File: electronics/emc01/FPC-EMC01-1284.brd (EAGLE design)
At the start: 160 x 100 mm, 87 parts, among them J10 CON-FFC-SFW15R, J4 PCIE, J9 CON-HDMI, Q4 16Mhz, SW1 SPST_TACT-EVQQ2, U1 LM2841, U10 MCP4728, U2 A4982, U3 A4982, U4 A4982, U5 ATMEGA1284P-AU, U7 AP7313

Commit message: Added pcb outline for FPC-EMC01-1284.brd, and placed connectors per AutoCAD DXF.  Added male 16-pin connector to firepick.lbr.
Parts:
- removed J3: (no value), pinhead-2:2X08SMD
- removed JP1: MOT-Y, SRG:JST_B4B-PH_HEADER
- removed JP10, JP11, JP8: (no value), pinhead-2:1X03SMD/90
- removed JP2: ICSP, pinhead-2:2X03SMD
- removed JP3: MOT-Z, SRG:JST_B4B-PH_HEADER
- removed JP4: (no value), pinhead-2:2X13SMD
- removed JP9: MOT-X, SRG:JST_B4B-PH_HEADER
- added J11, J12, J13, J14, J15: CONN-RECT-16PIN-2ROW, FirePick:CONN-RECT-2.54MM-16PIN-2ROW-SMTH
- added J2: PCIE, printrbot:5566-6
- added J8: CONN-RECT-3PINJST_PH_2MM, FirePick:CONN-JST_PH-2.0MM-3PIN-SMT-RA
- J1: value (none) -> CONN-RECT-26PIN-2ROWSHROUDED; device pinhead-2:2X08SMD -> FirePick:CONN-RECT-2.54MM-26-PIN-ROW-SHROUDED-SMTH
- J10: value CON-FFC-SFW15R -> ICSP; device !NJ SMT:CON-FFC-SFW15R -> FirePick:CONN-RECT-2.54MM-6-PIN-2ROW-SMTH
- J4: value PCIE -> MOT-X; device printrbot:5566-6 -> FirePick:CONN-JST-PH_2.0MM_4PIN-SMT-RA
- J5: value (none) -> MOT-Y; device pinhead-2:2X08SMD -> FirePick:CONN-JST-PH_2.0MM_4PIN-SMT-RA
- J6: value (none) -> MOT-Z; device pinhead-2:2X08SMD -> FirePick:CONN-JST-PH_2.0MM_4PIN-SMT-RA
- J7: value (none) -> CONN-RECT-3PINJST_PH_2MM; device pinhead-2:2X08SMD -> FirePick:CONN-JST_PH-2.0MM-3PIN-SMT-RA
- J9: value CON-HDMI -> CONN-RECT-3PINJST_PH_2MM; device !NJ SMT:CON-HDMI-FCI-10029449-001RLF -> FirePick:CONN-JST_PH-2.0MM-3PIN-SMT-RA
- moved JP5 443.2 mm to (88.9, 12.7)
- moved JP6 421.3 mm to (94.0, 25.4)
- moved J9 404.1 mm to (86.5, 37.2), turned to 240 degrees
- moved JP7 385.2 mm to (25.4, 15.2)
- moved J7 371.1 mm to (63.5, 88.0)
- moved J10 338.4 mm to (2.54, 16.5)
- moved LED2 327.2 mm to (7.62, 6.35)
- moved R6 327.2 mm to (1.27, 6.35)
- moved C9 327.2 mm to (12.7, 16.5)
- moved J6 317.5 mm to (79.3, 24.8), turned to 240 degrees
- moved J5 275.5 mm to (20.7, 24.8), turned to 120 degrees
- moved J1 273.4 mm to (50.0, 14.7)
- moved C11 217.5 mm to (97.8, 76.2)
- moved C13 217.5 mm to (97.8, 72.4)
- moved C14 217.5 mm to (97.8, 68.6)
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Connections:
- removed net CAM1_CN: J10.8, J9.12
- removed net CAM1_CP: J10.9, J9.10
- removed net CAM1_DN0: J10.2, J9.9
- removed net CAM1_DN1: J10.5, J9.6
- removed net CAM1_DP0: J10.3, J9.7
- removed net CAM1_DP1: J10.6, J9.4
- removed net CAM_CLK: J10.12, J9.1
- removed net CAM_GPIO: J10.11, J9.19
- removed net SCL0: J10.13, J9.15
- removed net SDA0: J10.14, J9.16
- net !~RESET: now also J10.2; no longer JP2.2
- net +3V3_RASPI: now also J1.1, J1.17, J15.2; no longer J7.2, JP4.1, JP4.17
- net +5V: now also J1.2, J1.4, J10.5, J11.14, J12.14, J12.7, J13.14, J13.8, J14.14, J14.7, J14.8, J15.1, J7.2, J8.2, J9.2; no longer J1.14, J10.15, J3.14, J3.7, J5.14, J5.8, J6.14, J6.7, J6.8, J7.1, J9.18, JP10.2, JP11.2, JP2.5, JP4.2, JP4.4, JP8.2
- net 12V: now also J11.1, J11.2, J12.1, J12.2, J13.1, J13.2, J14.1, J14.2, J2.1, J2.2, J2.3; no longer J1.1, J1.2, J3.1, J3.2, J4.1, J4.2, J4.3, J5.1, J5.2, J6.1, J6.2
- net GND: now also J1.14, J1.20, J1.25, J1.6, J1.9, J11.15, J11.16, J11.3, J11.4, J11.7, J11.8, J12.15, J12.16, J12.3, J12.4, J12.8, J13.15, J13.16, J13.3, J13.4, J13.7, J14.15, J14.16, J14.3, J14.4, J15.16, J15.3, J2.4, J2.5, J2.6, J8.3; no longer J1.15, J1.16, J1.3, J1.4, J1.7, J1.8, J10.10, J10.4, J10.7, J3.15, J3.16, J3.3, J3.4, J3.8, J4.4, J4.5, J4.6, J5.15, J5.16, J5.3, J5.4, J5.7, J6.15, J6.16, J6.3, J6.4, J7.16, J9.11, J9.13, J9.14, J9.17, J9.2, J9.5, J9.8, JP10.3, JP11.3, JP2.1, JP4.14, JP4.20, JP4.25, JP4.6, JP4.9, JP8.3
- net LCD_/E: now also J1.18, J15.7; no longer J7.7, JP4.18
- net LCD_DB4: now also J1.16, J15.9; no longer J7.9, JP4.16
- net LCD_DB5: now also J1.11, J15.10; no longer J7.10, JP4.11
- net LCD_DB6: now also J1.13, J15.11; no longer J7.11, JP4.13
- net LCD_DB7: now also J1.15, J15.12; no longer J7.12, JP4.15
- net LCD_RS: now also J1.22, J15.8; no longer J7.8, JP4.22
- net MISO: now also J10.6; no longer JP2.6
- net MOSI: now also J10.3; no longer JP2.3
- net N$10: now also J4.4; no longer JP9.P4
- net N$17: now also J4.3; no longer JP9.P3
- net N$20: now also J4.2; no longer JP9.P2
- net N$23: now also J4.1; no longer JP9.P1
- net N$24: now also J5.3; no longer JP1.P3
- net N$25: now also J5.4; no longer JP1.P4
- net N$26: now also J5.2; no longer JP1.P2
- net N$31: now also J5.1; no longer JP1.P1
- net N$39: now also J6.4; no longer JP3.P4
- net N$40: now also J6.3; no longer JP3.P3
- net N$41: now also J6.2; no longer JP3.P2
- net N$53: now also J6.1; no longer JP3.P1
- net PANEL_ENC_A: now also J1.26, J15.5; no longer J7.5, JP4.26
- net PANEL_ENC_B: now also J1.21, J15.6; no longer J7.6, JP4.21
- net PANEL_ENC_SW: now also J1.24, J15.4; no longer J7.4, JP4.24
- net PANEL_LED_GRN: now also J1.19, J15.13; no longer J7.13, JP4.19
- net PANEL_LED_RED: now also J1.12, J15.14; no longer J7.14, JP4.12
- net PANEL_PUSHBTN: now also J1.23, J15.15; no longer J7.15, JP4.23
- net RASPI_RXD: now also J1.10; no longer JP4.10
- net RASPI_TXD: now also J1.8; no longer JP4.8
- net SCL: now also J11.6, J12.6, J13.6, J14.6; no longer J1.6, J3.6, J5.6, J6.6
- net SCLK: now also J10.4; no longer JP2.4
- net SDA: now also J11.5, J12.5, J13.5, J14.5; no longer J1.5, J3.5, J5.5, J6.5
- net TOOL1_AIN: now also J11.13; no longer J1.13
- net TOOL1_DOUT: now also J11.12; no longer J1.12
- net TOOL1_ENABLE: now also J11.9; no longer J1.9
- net TOOL2_AIN: now also J12.13; no longer J3.13
- net TOOL2_DOUT: now also J12.12; no longer J3.12
- net TOOL2_ENABLE: now also J12.9; no longer J3.9
- net TOOL3_AIN: now also J13.13; no longer J5.13
- net TOOL3_DOUT: now also J13.12; no longer J5.12
- net TOOL3_ENABLE: now also J13.9; no longer J5.9
- net TOOL4_AIN: now also J14.13; no longer J6.13
- net TOOL4_DOUT: now also J14.12; no longer J6.12
- net TOOL4_ENABLE: now also J14.9; no longer J6.9
- net TOOL_DIR: now also J11.11, J12.11, J13.11, J14.11; no longer J1.11, J3.11, J5.11, J6.11
- net TOOL_STEP: now also J11.10, J12.10, J13.10, J14.10; no longer J1.10, J3.10, J5.10, J6.10
- net X-STOP: now also J7.1; no longer JP8.1
- net Y-STOP: now also J8.1; no longer JP10.1
- net Z-STOP: now also J9.1; no longer JP11.1
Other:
- board size 160 x 100 mm -> 100 x 86.6 mm

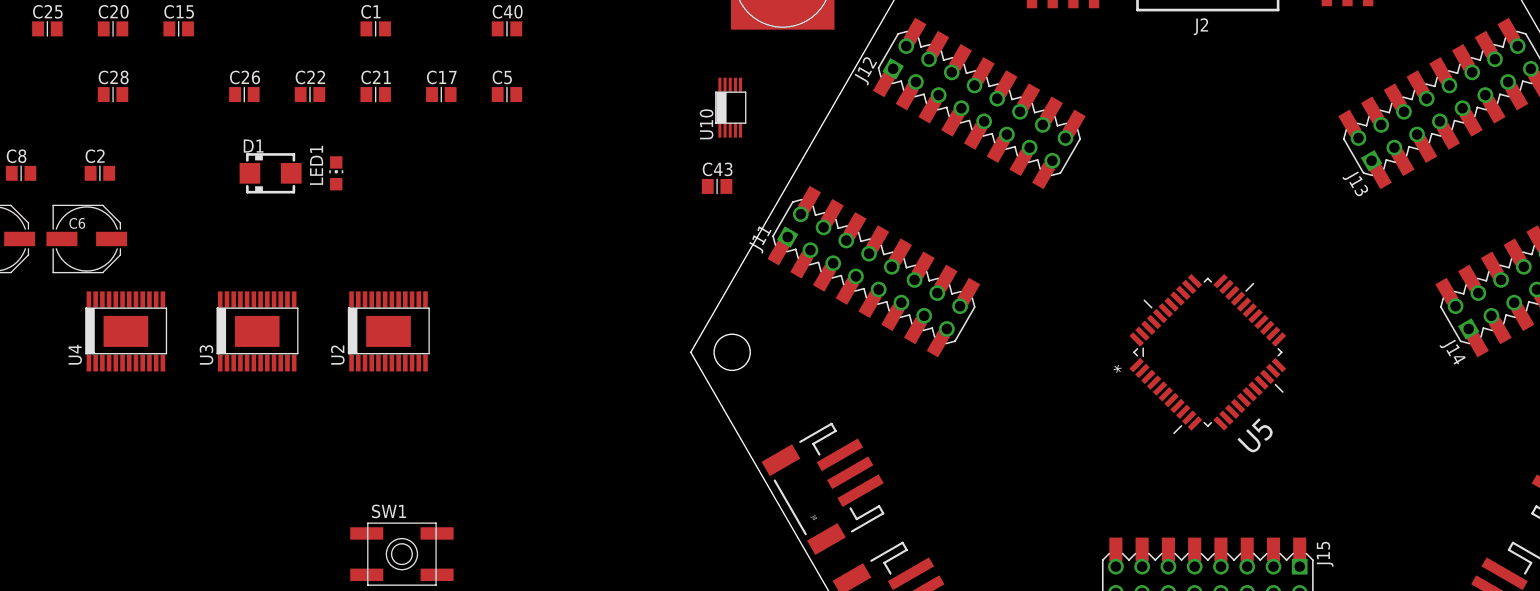
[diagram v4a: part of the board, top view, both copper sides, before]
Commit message: Moved stepper driver IC's to symmetrically-pleasing locations
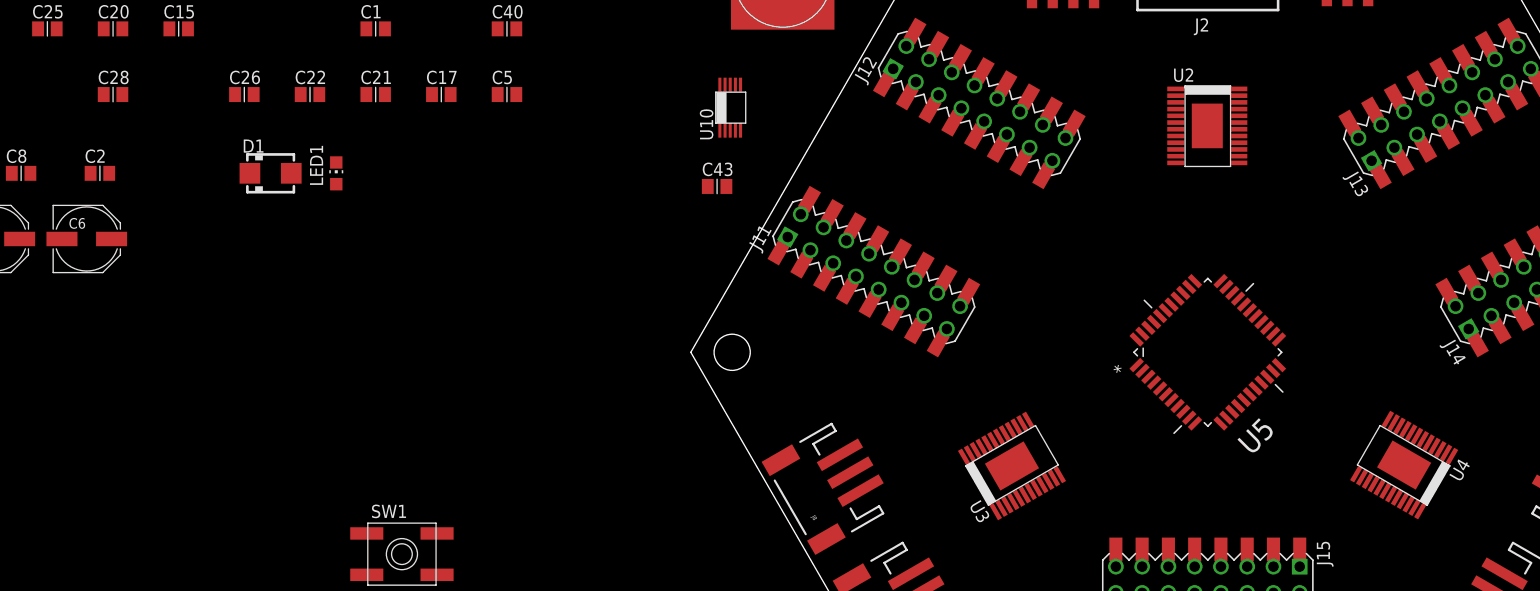
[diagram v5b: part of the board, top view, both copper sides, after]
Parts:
- moved U4 124.2 mm to (68.9, 39.1), turned to 150 degrees
- moved U2 81.6 mm to (50.0, 71.9), turned to 270 degrees
- moved U3 74.1 mm to (31.1, 39.1), turned to 30 degrees

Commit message: minor tweaks before layout
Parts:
- removed C32: 10uF, ipc-7351-capacitor:CAPC2012X145AN
- removed JP6: (no value), pinhead-2:1X06SMD
- removed JP7: (no value), pinhead-2:1X02SMD
- removed LED1: PWR, led:CHIP-LED0805
- removed R1: 330, adafruit:R0805
- removed U7: AP7313, printrbot:SOT23C
- added J16: (no value), !con-lstb:MA02-1
- added J3: (no value), !con-lstb:MA06-1
- JP5: device pinhead-2:1X04SMD -> !con-lstb:MA04-1
- moved J6 14.4 mm to (86.5, 37.2)
- moved J9 14.4 mm to (79.3, 24.8)
- moved JP5 5.68 mm to (94.0, 15.2)
- turned U2 to 90 degrees
- turned U3 to 210 degrees
- turned U4 to 330 degrees
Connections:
- removed net +3V3: C32.1, U7.2
- removed net N$1: LED1.A, R1.1
- net +5V: now also J3.4; no longer JP6.4, R1.2, U7.1
- net AVR_RXD: now also J3.3; no longer JP6.3
- net AVR_TXD: now also J3.2; no longer JP6.2
- net DTR: now also J3.1; no longer JP6.1
- net GND: now also J3.5, J3.6; no longer C32.2, JP6.5, JP6.6, LED1.C, U7.3
- net N$17: now also J4.2; no longer J4.3
- net N$20: now also J4.3; no longer J4.2
- net N$24: now also J5.2; no longer J5.3
- net N$26: now also J5.3; no longer J5.2
- net N$40: now also J6.2; no longer J6.3
- net N$41: now also J6.3; no longer J6.2
- net RASPI_RXD: now also J16.1; no longer JP7.1
- net RASPI_TXD: now also J16.2; no longer JP7.2

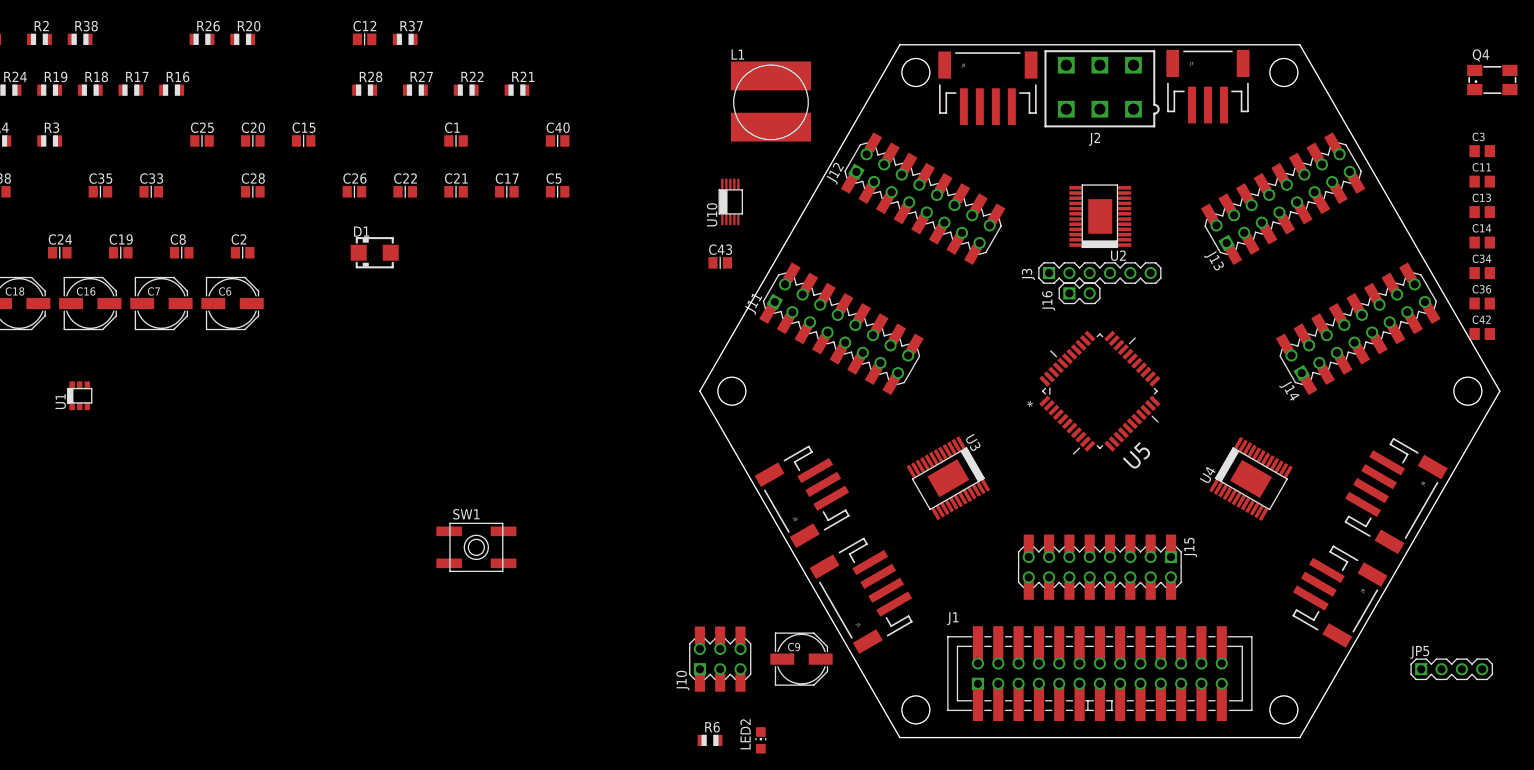
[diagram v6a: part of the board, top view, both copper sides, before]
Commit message: Routed J15-J1
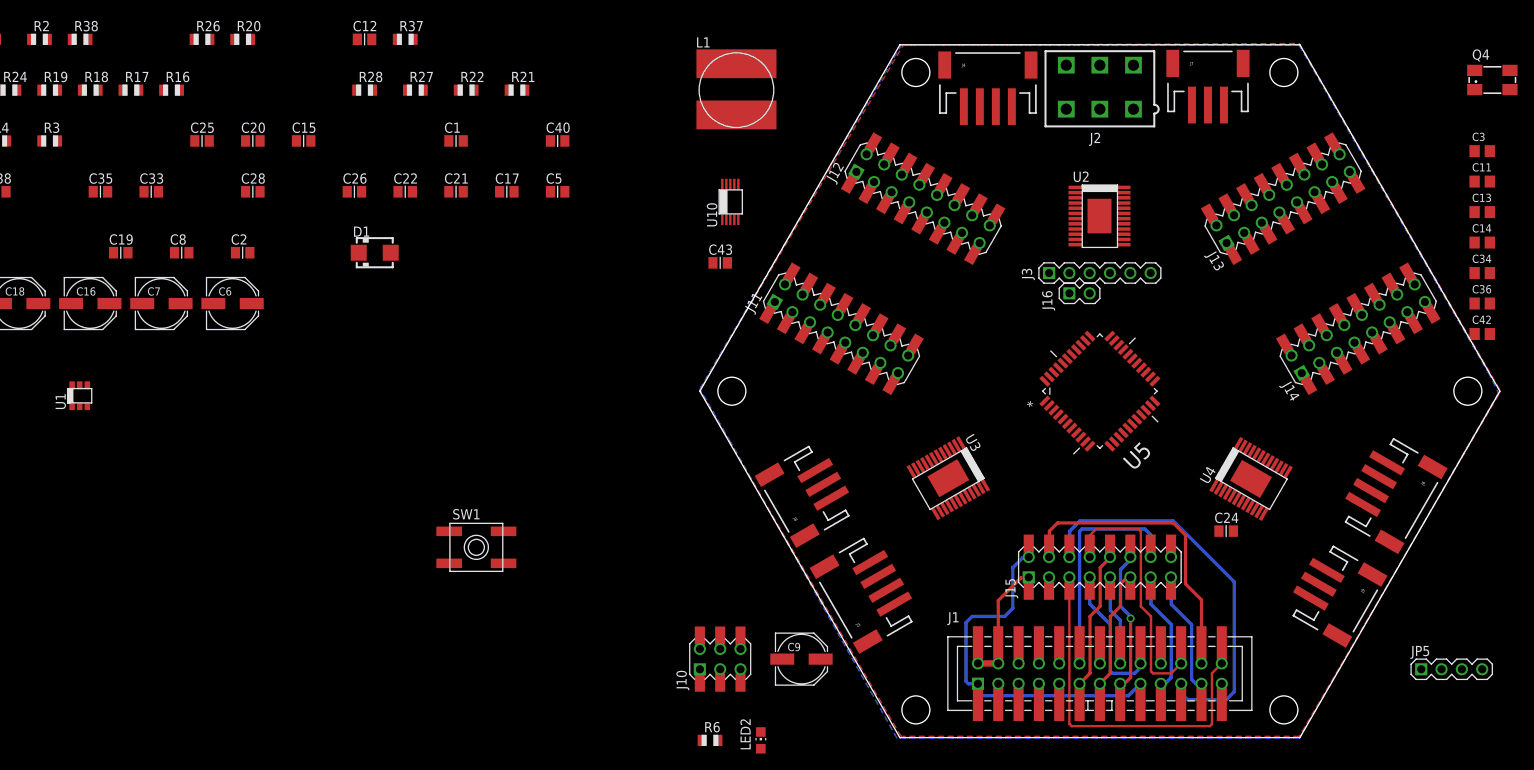
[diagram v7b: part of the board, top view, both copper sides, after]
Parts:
- moved C24 149.9 mm to (65.8, 32.5)
- moved L1 4.58 mm to (4.57, 87.9)
- turned J15 to 0 degrees
- turned U2 to 270 degrees
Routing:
- net PANEL_ENC_B: track 0.00 -> 49.8 mm
- net +3V3_RASPI: track 0.00 -> 45.3 mm
- net PANEL_ENC_A: track 0.00 -> 44.5 mm
- net PANEL_ENC_SW: track 0.00 -> 38.2 mm
- net LCD_RS: track 0.00 -> 32.0 mm
- net PANEL_LED_RED: track 0.00 -> 28.6 mm
- net LCD_DB7: track 0.00 -> 17.7 mm, vias 0 -> 1
- net LCD_/E: track 0.00 -> 17.5 mm
- net LCD_DB5: track 0.00 -> 17.4 mm
- net +5V: track 0.00 -> 15.4 mm
- net PANEL_PUSHBTN: track 0.00 -> 15.3 mm
- net PANEL_LED_GRN: track 0.00 -> 15.2 mm
- net LCD_DB6: track 0.00 -> 15.1 mm
- net LCD_DB4: track 0.00 -> 11.3 mm
- added copper zone on layer 1, net +5V
- added copper zone on layer 16, net GND
